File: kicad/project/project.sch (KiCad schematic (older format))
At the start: 41 parts, among them J1 SWD, Q1 MMBT3906, Q2 MMBT3906, Q3 IRF3205, Q4 MMBT3904, U1 NCV4264-2CST33T3G, U2 STM32L031F4Px

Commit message: Initial board layout
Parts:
- removed H2, H3, H4: MountingHole_Pad, MountingHole:MountingHole_3.2mm_M3_Pad, symbol Mechanical:MountingHole_Pad
- R7: value 4K7 -> 1K
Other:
- note added: "EMI surpression\n(not strictly needed)"
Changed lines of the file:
@@
-$EndComp
-$Comp
-L Mechanical:MountingHole_Pad H2
-U 1 1 5C8B1717
-P 3300 6625
-F 0 "H2" H 3400 6676 50  0000 L CNN
-F 1 "MountingHole_Pad" H 3400 6585 50  0000 L CNN
-F 2 "MountingHole:MountingHole_3.2mm_M3_Pad" H 3300 6625 50  0001 C CNN
-F 3 "~" H 3300 6625 50  0001 C CNN
-	1    3300 6625
-	1    0    0    -1
-$EndComp
-$Comp
-L Mechanical:MountingHole_Pad H3
-U 1 1 5C8B74C5
-P 2275 7250
-F 0 "H3" H 2375 7301 50  0000 L CNN
-F 1 "MountingHole_Pad" H 2375 7210 50  0000 L CNN
-F 2 "MountingHole:MountingHole_3.2mm_M3_Pad" H 2275 7250 50  0001 C CNN
-F 3 "~" H 2275 7250 50  0001 C CNN
-	1    2275 7250
-	1    0    0    -1
-$EndComp
-$Comp
-L Mechanical:MountingHole_Pad H4
-U 1 1 5C8B74CC
-P 3300 7250
-F 0 "H4" H 3400 7301 50  0000 L CNN
-F 1 "MountingHole_Pad" H 3400 7210 50  0000 L CNN
-F 2 "MountingHole:MountingHole_3.2mm_M3_Pad" H 3300 7250 50  0001 C CNN
-F 3 "~" H 3300 7250 50  0001 C CNN
-	1    3300 7250
-	1    0    0    -1
 $EndComp
 $Comp
@@
 F 3 "" H 2275 6725 50  0001 C CNN
 	1    2275 6725
-	1    0    0    -1
-$EndComp
-$Comp
-L power:GND #PWR024
-U 1 1 5C8BA36C
-P 3300 6725
-F 0 "#PWR024" H 3300 6475 50  0001 C CNN
-F 1 "GND" H 3305 6552 50  0000 C CNN
-F 2 "" H 3300 6725 50  0001 C CNN
-F 3 "" H 3300 6725 50  0001 C CNN
-	1    3300 6725
-	1    0    0    -1
-$EndComp
-$Comp
-L power:GND #PWR026
-U 1 1 5C8BA3D3
-P 3300 7350
-F 0 "#PWR026" H 3300 7100 50  0001 C CNN
-F 1 "GND" H 3305 7177 50  0000 C CNN
-F 2 "" H 3300 7350 50  0001 C CNN
-F 3 "" H 3300 7350 50  0001 C CNN
-	1    3300 7350
-	1    0    0    -1
-$EndComp
-$Comp
-L power:GND #PWR025
-U 1 1 5C8BA43A
-P 2275 7350
-F 0 "#PWR025" H 2275 7100 50  0001 C CNN
-F 1 "GND" H 2280 7177 50  0000 C CNN
-F 2 "" H 2275 7350 50  0001 C CNN
-F 3 "" H 2275 7350 50  0001 C CNN
-	1    2275 7350
 	1    0    0    -1
 $EndComp
@@
 P 8325 4575
 F 0 "R7" V 8118 4575 50  0000 C CNN
-F 1 "4K7" V 8209 4575 50  0000 C CNN
+F 1 "1K" V 8209 4575 50  0000 C CNN
 F 2 "Resistor_SMD:R_0603_1608Metric_Pad1.05x0.95mm_HandSolder" V 8255 4575 50  0001 C CNN
 F 3 "~" H 8325 4575 50  0001 C CNN
@@
 Text Label 2050 1200 0    50   ~ 0
 REG_IN
+Text Notes 8075 4775 0    39   Italic 0
+EMI surpression\n(not strictly needed)
 $EndSCHEMATC

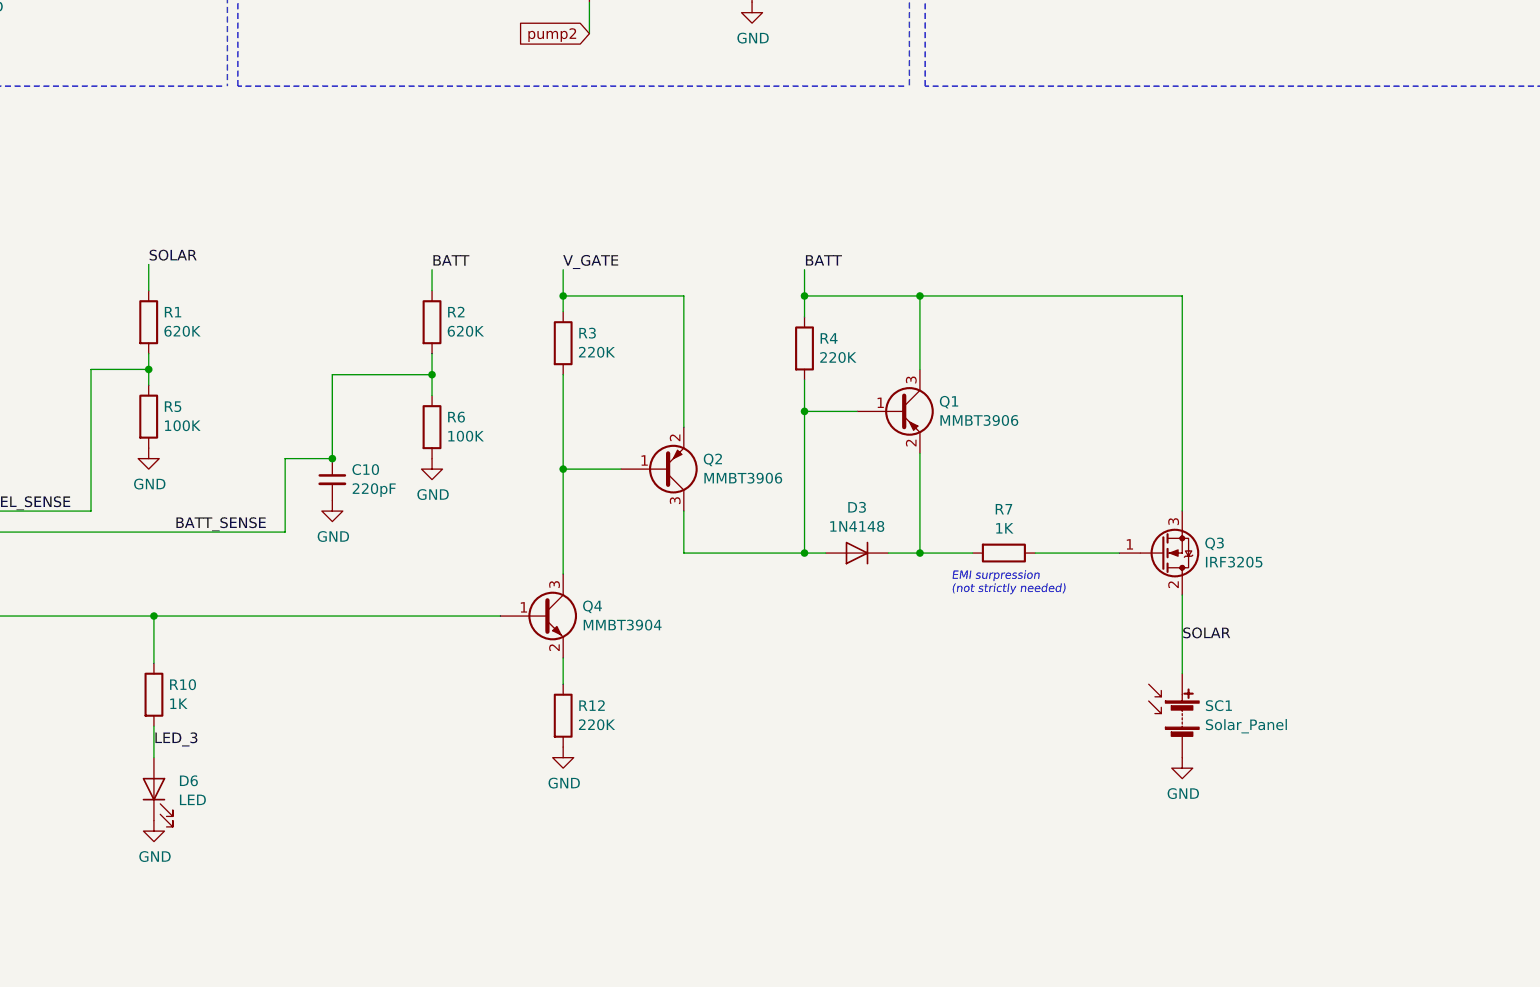
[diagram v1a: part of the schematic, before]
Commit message: Clearer schematic
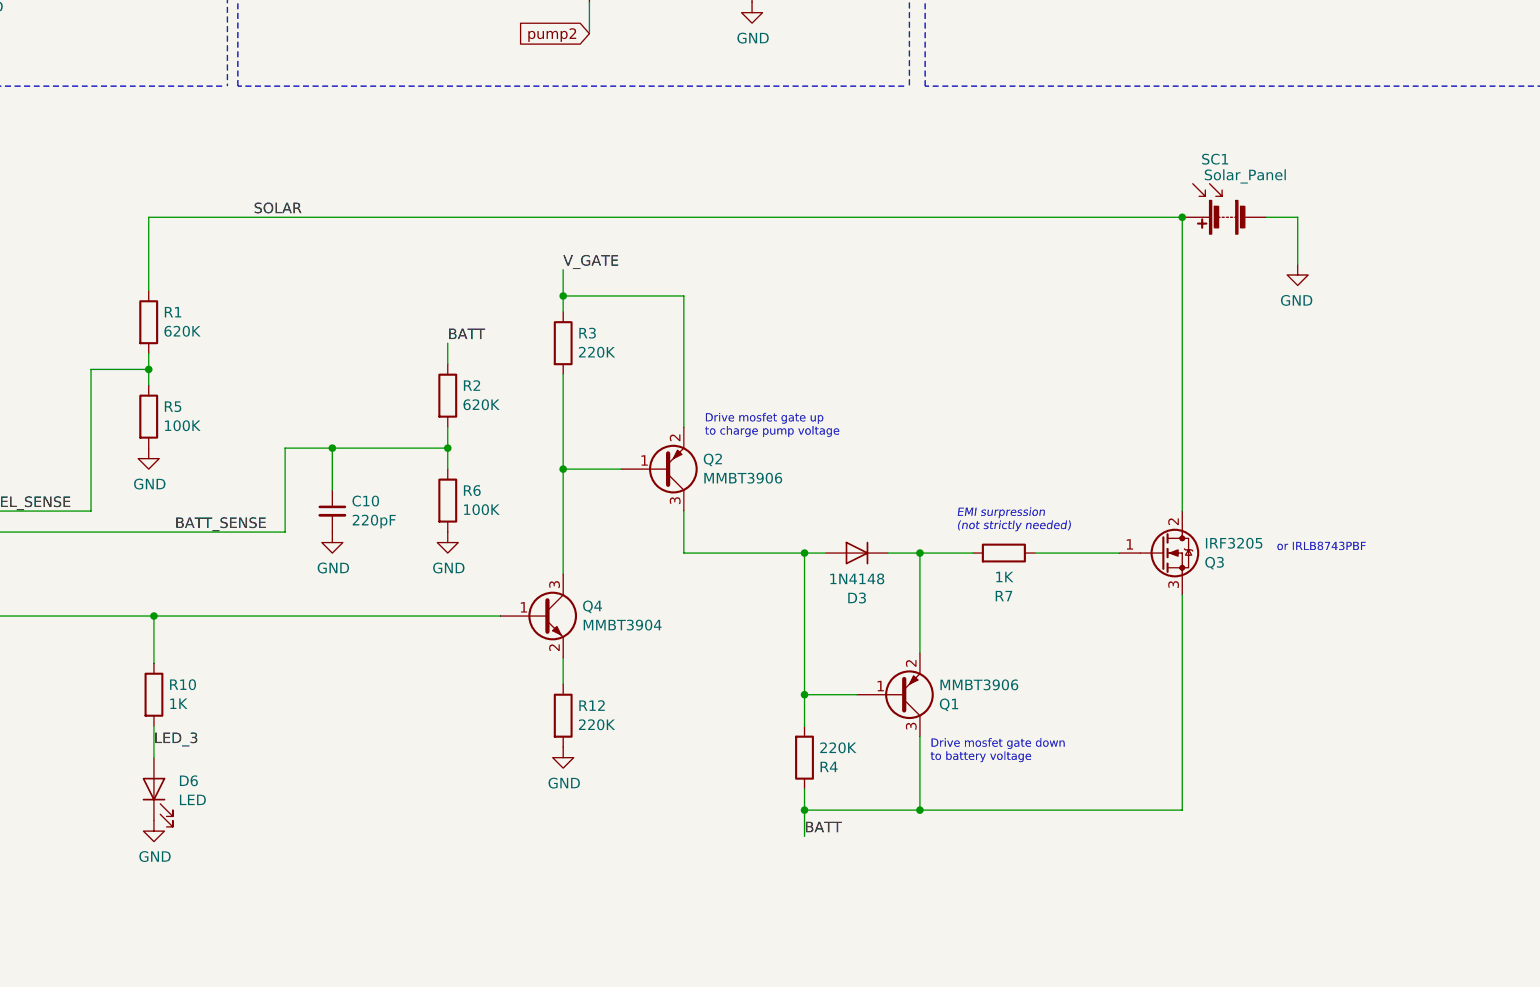
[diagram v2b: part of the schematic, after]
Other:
- note added: "Drive mosfet gate down\nto battery voltage"
- note added: "Drive mosfet gate up \nto charge pump voltage"
- note added: "or IRLB8743PBF"
- moved on the sheet: C10, Q1, R2, R4, R6, SC1
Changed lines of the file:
@@
 L Device:R R6
 U 1 1 5C7C5AEB
-P 5600 3975
-F 0 "R6" H 5670 4021 50  0000 L CNN
-F 1 "100K" H 5670 3930 50  0000 L CNN
-F 2 "Resistor_SMD:R_0603_1608Metric_Pad1.05x0.95mm_HandSolder" V 5530 3975 50  0001 C CNN
-F 3 "~" H 5600 3975 50  0001 C CNN
-	1    5600 3975
+P 5675 4325
+F 0 "R6" H 5745 4371 50  0000 L CNN
+F 1 "100K" H 5745 4280 50  0000 L CNN
+F 2 "Resistor_SMD:R_0603_1608Metric_Pad1.05x0.95mm_HandSolder" V 5605 4325 50  0001 C CNN
+F 3 "~" H 5675 4325 50  0001 C CNN
+	1    5675 4325
 	1    0    0    -1
 $EndComp
@@
 L Device:R R2
 U 1 1 5C7C5BA1
-P 5600 3475
-F 0 "R2" H 5670 3521 50  0000 L CNN
-F 1 "620K" H 5670 3430 50  0000 L CNN
-F 2 "Resistor_SMD:R_0603_1608Metric_Pad1.05x0.95mm_HandSolder" V 5530 3475 50  0001 C CNN
-F 3 "~" H 5600 3475 50  0001 C CNN
-	1    5600 3475
-	1    0    0    -1
-$EndComp
-Wire Wire Line
-	5600 3625 5600 3725
-Connection ~ 5600 3725
-Wire Wire Line
-	5600 3725 5600 3825
+P 5675 3825
+F 0 "R2" H 5745 3871 50  0000 L CNN
+F 1 "620K" H 5745 3780 50  0000 L CNN
+F 2 "Resistor_SMD:R_0603_1608Metric_Pad1.05x0.95mm_HandSolder" V 5605 3825 50  0001 C CNN
+F 3 "~" H 5675 3825 50  0001 C CNN
+	1    5675 3825
+	1    0    0    -1
+$EndComp
+Wire Wire Line
+	5675 3975 5675 4075
+Connection ~ 5675 4075
+Wire Wire Line
+	5675 4075 5675 4175
 $Comp
 L power:GND #PWR015
 U 1 1 5C7C73C4
-P 5600 4125
-F 0 "#PWR015" H 5600 3875 50  0001 C CNN
-F 1 "GND" H 5605 3952 50  0000 C CNN
-F 2 "" H 5600 4125 50  0001 C CNN
-F 3 "" H 5600 4125 50  0001 C CNN
-	1    5600 4125
+P 5675 4475
+F 0 "#PWR015" H 5675 4225 50  0001 C CNN
+F 1 "GND" H 5680 4302 50  0000 C CNN
+F 2 "" H 5675 4475 50  0001 C CNN
+F 3 "" H 5675 4475 50  0001 C CNN
+	1    5675 4475
 	1    0    0    -1
 $EndComp
@@
 L Device:C_Small C10
 U 1 1 5C7CB72F
-P 5125 4225
-F 0 "C10" H 5217 4271 50  0000 L CNN
-F 1 "220pF" H 5217 4180 50  0000 L CNN
-F 2 "Capacitor_SMD:C_0603_1608Metric_Pad1.05x0.95mm_HandSolder" H 5125 4225 50  0001 C CNN
-F 3 "~" H 5125 4225 50  0001 C CNN
-	1    5125 4225
+P 5125 4375
+F 0 "C10" H 5217 4421 50  0000 L CNN
+F 1 "220pF" H 5217 4330 50  0000 L CNN
+F 2 "Capacitor_SMD:C_0603_1608Metric_Pad1.05x0.95mm_HandSolder" H 5125 4375 50  0001 C CNN
+F 3 "~" H 5125 4375 50  0001 C CNN
+	1    5125 4375
 	1    0    0    -1
 $EndComp
@@
 L power:GND #PWR016
 U 1 1 5C7CB7D1
-P 5125 4325
-F 0 "#PWR016" H 5125 4075 50  0001 C CNN
-F 1 "GND" H 5130 4152 50  0000 C CNN
-F 2 "" H 5125 4325 50  0001 C CNN
-F 3 "" H 5125 4325 50  0001 C CNN
-	1    5125 4325
-	1    0    0    -1
-$EndComp
-Wire Wire Line
-	5125 3725 5600 3725
+P 5125 4475
+F 0 "#PWR016" H 5125 4225 50  0001 C CNN
+F 1 "GND" H 5130 4302 50  0000 C CNN
+F 2 "" H 5125 4475 50  0001 C CNN
+F 3 "" H 5125 4475 50  0001 C CNN
+	1    5125 4475
+	1    0    0    -1
+$EndComp
 $Comp
 L Device:R R1
@@
 $EndComp
 Wire Wire Line
-	5600 3225 5600 3325
+	5675 3575 5675 3675
 Text Label 3275 4875 0    50   ~ 0
 PWM
@@
 L Device:Solar_Cells SC1
 U 1 1 5C80516E
-P 9175 5350
-F 0 "SC1" H 9283 5396 50  0000 L CNN
-F 1 "Solar_Panel" H 9283 5305 50  0000 L CNN
-F 2 "TerminalBlock:TerminalBlock_bornier-2_P5.08mm" V 9175 5410 50  0001 C CNN
-F 3 "~" V 9175 5410 50  0001 C CNN
-	1    9175 5350
-	1    0    0    -1
+P 9375 2975
+F 0 "SC1" V 9100 2950 50  0000 L CNN
+F 1 "Solar_Panel" V 9175 2675 50  0000 L CNN
+F 2 "TerminalBlock:TerminalBlock_bornier-2_P5.08mm" V 9375 3035 50  0001 C CNN
+F 3 "~" V 9375 3035 50  0001 C CNN
+	1    9375 2975
+	0    -1   1    0
 $EndComp
 Wire Wire Line
@@
 	1    0    0    -1
 $EndComp
-Wire Wire Line
-	4900 4475 4900 4125
-Wire Wire Line
-	4900 4125 5125 4125
-Wire Wire Line
-	5125 3725 5125 4125
-Connection ~ 5125 4125
 Wire Wire Line
 	2800 4475 4900 4475
@@
 Wire Wire Line
 	7125 1225 7675 1225
-Text Label 5600 3225 0    50   ~ 0
+Text Label 5675 3575 0    50   ~ 0
 BATT
-Wire Wire Line
-	9175 5150 9175 4775
-Text Label 9175 5000 0    50   ~ 0
+Text Label 4750 2975 0    50   ~ 0
 SOLAR
-Text Label 4250 3200 0    50   ~ 0
-SOLAR
-Wire Wire Line
-	4250 3200 4250 3325
 $Comp
 L Device:R R3
@@
 L Device:R R4
 U 1 1 5CDCC025
-P 7375 3600
-F 0 "R4" H 7445 3646 50  0000 L CNN
-F 1 "220K" H 7445 3555 50  0000 L CNN
-F 2 "Resistor_SMD:R_0603_1608Metric_Pad1.05x0.95mm_HandSolder" V 7305 3600 50  0001 C CNN
-F 3 "~" H 7375 3600 50  0001 C CNN
-	1    7375 3600
-	1    0    0    -1
+P 7375 5550
+F 0 "R4" H 7445 5596 50  0000 L CNN
+F 1 "220K" H 7445 5505 50  0000 L CNN
+F 2 "Resistor_SMD:R_0603_1608Metric_Pad1.05x0.95mm_HandSolder" V 7305 5550 50  0001 C CNN
+F 3 "~" H 7375 5550 50  0001 C CNN
+	1    7375 5550
+	1    0    0    1
 $EndComp
 $Comp
@@
 L Transistor_BJT:MMBT3906 Q1
 U 1 1 5CDDBCFD
-P 7825 3900
-F 0 "Q1" H 8016 3946 50  0000 L CNN
-F 1 "MMBT3906" H 8016 3855 50  0000 L CNN
-F 2 "Package_TO_SOT_SMD:SOT-23" H 8025 3825 50  0001 L CIN
-F 3 "https://www.fairchildsemi.com/datasheets/2N/2N3906.pdf" H 7825 3900 50  0001 L CNN
-	1    7825 3900
-	1    0    0    -1
-$EndComp
-Wire Wire Line
-	7375 3900 7625 3900
-Wire Wire Line
-	7375 3900 7375 4575
+P 7825 5250
+F 0 "Q1" H 8016 5296 50  0000 L CNN
+F 1 "MMBT3906" H 8016 5205 50  0000 L CNN
+F 2 "Package_TO_SOT_SMD:SOT-23" H 8025 5175 50  0001 L CIN
+F 3 "https://www.fairchildsemi.com/datasheets/2N/2N3906.pdf" H 7825 5250 50  0001 L CNN
+	1    7825 5250
+	1    0    0    1
+$EndComp
+Wire Wire Line
+	7375 5250 7625 5250
+Wire Wire Line
+	7375 5250 7375 4575
 Wire Wire Line
 	7375 4575 6800 4575
 Wire Wire Line
 	6800 4575 6800 4375
-Text Label 7375 3225 0    50   ~ 0
+Text Label 7375 5925 0    50   ~ 0
 BATT
 Wire Wire Line
-	7375 3225 7375 3350
-Wire Wire Line
-	7375 3750 7375 3900
-Connection ~ 7375 3900
-Wire Wire Line
-	7925 3700 7925 3350
-Wire Wire Line
-	7925 3350 7375 3350
-Connection ~ 7375 3350
-Wire Wire Line
-	7375 3350 7375 3450
+	7375 5925 7375 5800
+Wire Wire Line
+	7375 5400 7375 5250
+Connection ~ 7375 5250
+Wire Wire Line
+	7925 5450 7925 5800
+Wire Wire Line
+	7925 5800 7375 5800
+Connection ~ 7375 5800
+Wire Wire Line
+	7375 5800 7375 5700
 $Comp
 L Diode:1N4148 D3
@@
 F 3 "http://www.nxp.com/documents/data_sheet/1N4148_1N4448.pdf" H 7625 4575 50  0001 C CNN
 	1    7625 4575
-	-1   0    0    1
-$EndComp
-Wire Wire Line
-	7925 4100 7925 4575
+	-1   0    0    -1
+$EndComp
+Wire Wire Line
+	7925 5050 7925 4575
 Wire Wire Line
 	7925 4575 7775 4575
@@
 F 3 "~" H 8325 4575 50  0001 C CNN
 	1    8325 4575
-	0    1    1    0
+	0    1    -1   0
 $EndComp
 $Comp
@@
 F 3 "http://www.irf.com/product-info/datasheets/data/irf3205.pdf" H 9075 4575 50  0001 L CNN
 	1    9075 4575
-	1    0    0    1
+	1    0    0    -1
 $EndComp
 Wire Wire Line
@@
 Connection ~ 7925 4575
 Wire Wire Line
-	9175 4375 9175 3350
-Wire Wire Line
-	9175 3350 7925 3350
-Connection ~ 7925 3350
+	9175 4775 9175 5800
+Wire Wire Line
+	9175 5800 7925 5800
+Connection ~ 7925 5800
 $Comp
 L power:GND #PWR019
 U 1 1 5CDF634C
-P 9175 5550
-F 0 "#PWR019" H 9175 5300 50  0001 C CNN
-F 1 "GND" H 9180 5377 50  0000 C CNN
-F 2 "" H 9175 5550 50  0001 C CNN
-F 3 "" H 9175 5550 50  0001 C CNN
-	1    9175 5550
-	1    0    0    -1
+P 9725 3200
+F 0 "#PWR019" H 9725 2950 50  0001 C CNN
+F 1 "GND" H 9730 3027 50  0000 C CNN
+F 2 "" H 9725 3200 50  0001 C CNN
+F 3 "" H 9725 3200 50  0001 C CNN
+	1    9725 3200
+	-1   0    0    -1
 $EndComp
 Connection ~ 4275 4875
@@
 Text Label 2050 1200 0    50   ~ 0
 REG_IN
-Text Notes 8075 4775 0    39   Italic 0
+Text Notes 8100 4475 0    39   Italic 0
 EMI surpression\n(not strictly needed)
+Wire Wire Line
+	5125 4075 5675 4075
+Wire Wire Line
+	5125 4075 5125 4275
+Wire Wire Line
+	4900 4475 4900 4075
+Wire Wire Line
+	4900 4075 5125 4075
+Connection ~ 5125 4075
+Wire Wire Line
+	9575 2975 9725 2975
+Wire Wire Line
+	9725 2975 9725 3200
+Text Notes 6900 4025 0    39   ~ 0
+Drive mosfet gate up \nto charge pump voltage
+Text Notes 7975 5575 0    39   ~ 0
+Drive mosfet gate down\nto battery voltage
+Text Notes 9625 4575 0    39   ~ 0
+or IRLB8743PBF
+Wire Wire Line
+	4250 2975 9175 2975
+Wire Wire Line
+	4250 2975 4250 3325
+Connection ~ 9175 2975
+Wire Wire Line
+	9175 2975 9175 4375
 $EndSCHEMATC
